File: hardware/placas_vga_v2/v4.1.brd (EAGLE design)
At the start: 32 x 39.9 mm, 39 parts

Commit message: Finalizo diseño
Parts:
- moved R2 0.64 mm to (18.8, 22.9)
- moved R22 0.64 mm to (18.8, 25.3)
- moved R3 0.64 mm to (18.8, 18.2)
- moved R6 0.64 mm to (18.8, 3.89)
- moved R7 0.64 mm to (18.8, 1.51)
- moved R24 0.63 mm to (18.8, 15.8)
- moved R25 0.63 mm to (18.8, 11.0)
- moved R26 0.63 mm to (18.8, 6.27)
- moved R4 0.63 mm to (18.8, 13.4)
- moved R5 0.63 mm to (18.8, 8.65)
- moved R1 0.63 mm to (18.8, 27.7), turned to 180 degrees
- moved R23 0.63 mm to (18.8, 20.6)
- moved R10 0.48 mm to (23.7, 18.3)
- moved R11 0.48 mm to (23.7, 13.6)
- moved R12 0.48 mm to (23.7, 8.81)
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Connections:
- removed net EXT11: R16.1
- removed net EXT14: R15.1
- removed net EXT2: R8.1
- removed net EXT3: R10.1
- removed net EXT4: R9.1
- removed net EXT5: R17.1
- removed net N$1: U$1.10, U$1.5, U$1.6, U$1.7, U$1.8, U$1.9
- removed net N$10: R12.1
- removed net N$11: R13.1
- removed net N$12: R18.1
- removed net N$13: R19.1
- removed net N$14: R20.1
- removed net N$9: R11.1
- net EXT18: now also R8.1
- net EXT19: now also R9.1
- net EXT21: now also R10.1
- net EXT22: now also R11.1
- net EXT24: now also R12.1
- net EXT25: now also R13.1
- net EXT27: now also R17.1
- net EXT28: now also R15.1
- net EXT30: now also R18.1
- net EXT31: now also R16.1
- net EXT33: now also R20.1
- net EXT34: now also R19.1
- net GND: now also U$1.10, U$1.5, U$1.6, U$1.7, U$1.8
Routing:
- net GND: track 12.4 -> 89.6 mm
- net EXT33: track 0.00 -> 37.4 mm
- net EXT24: track 0.00 -> 36.1 mm
- net EXT25: track 0.00 -> 34.2 mm
- net EXT30: track 0.00 -> 29.1 mm
- net EXT21: track 0.00 -> 28.2 mm
- net EXT34: track 0.00 -> 26.4 mm
- net EXT22: track 0.00 -> 26.2 mm
- net EXT27: track 0.00 -> 26.2 mm
- net N$41: track 2.38 -> 21.0 mm, vias 0 -> 1
- net EXT18: track 0.00 -> 18.5 mm
- net EXT19: track 0.00 -> 18.3 mm
- net EXT31: track 0.00 -> 13.1 mm
- net GREEN: track 2.38 -> 15.4 mm, vias 0 -> 1
- net EXT28: track 0.00 -> 8.75 mm
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- added copper zone on layer 1, net GND

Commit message: Añado sd2iec
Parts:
- renumbered U$1 to VGA
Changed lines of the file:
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@@
 <element name="J12" library="pinhead" package="1X12" value="" x="16.51" y="32.940625"/>
 <element name="J10" library="pinhead" package="1X12" value="" x="16.51" y="38.020625"/>
-<element name="U$1" library="SparkFun-Connectors" package="DB15" value="DB15" x="6.6675" y="15.478125" rot="MR270"/>
+<element name="VGA" library="SparkFun-Connectors" package="DB15" value="DB15" x="6.6675" y="15.478125" rot="MR270"/>
 <element name="R1" library="rcl" package="R0805" value="511" x="18.811875" y="27.701875" rot="MR180"/>
 <element name="R2" library="rcl" package="R0805" value="511" x="18.811875" y="22.939375" rot="MR0"/>
@@
 <wire x1="24.683125" y1="1.666875" x2="24.683125" y2="0.875625" width="0.254" layer="16"/>
 <wire x1="24.683125" y1="0.875625" x2="24.685625" y2="0.873125" width="0.254" layer="16"/>
-<contactref element="U$1" pad="7"/>
-<contactref element="U$1" pad="8"/>
-<contactref element="U$1" pad="10"/>
-<contactref element="U$1" pad="5"/>
-<contactref element="U$1" pad="6"/>
+<contactref element="VGA" pad="7"/>
+<contactref element="VGA" pad="8"/>
+<contactref element="VGA" pad="10"/>
+<contactref element="VGA" pad="5"/>
+<contactref element="VGA" pad="6"/>
 <wire x1="14.2875" y1="10.638125" x2="12.8875" y2="10.638125" width="0.254" layer="16"/>
 <wire x1="12.8875" y1="10.638125" x2="11.7475" y2="11.778125" width="0.254" layer="16"/>
@@
 </signal>
 <signal name="GREEN">
-<contactref element="U$1" pad="2"/>
+<contactref element="VGA" pad="2"/>
 <contactref element="R8" pad="2"/>
 <contactref element="R27" pad="1"/>
@@
 </signal>
 <signal name="HSYNC">
-<contactref element="U$1" pad="13"/>
+<contactref element="VGA" pad="13"/>
 <contactref element="J12" pad="2"/>
 <wire x1="5.08" y1="32.940625" x2="5.08" y2="19.345625" width="0.254" layer="16"/>
@@
 </signal>
 <signal name="VSYNC">
-<contactref element="U$1" pad="14"/>
+<contactref element="VGA" pad="14"/>
 <contactref element="J10" pad="1"/>
 <wire x1="2.54" y1="38.020625" x2="2.54" y2="34.925" width="0.254" layer="16"/>
@@
 </signal>
 <signal name="N$16">
-<contactref element="U$1" pad="1"/>
+<contactref element="VGA" pad="1"/>
 <contactref element="R1" pad="2"/>
 <contactref element="R22" pad="1"/>
@@
 <signal name="N$41">
 <contactref element="R15" pad="2"/>
-<contactref element="U$1" pad="3"/>
+<contactref element="VGA" pad="3"/>
 <contactref element="R32" pad="1"/>
 <wire x1="27.704375" y1="28.336875" x2="27.704375" y2="25.955625" width="0.254" layer="16"/>

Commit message: Actualizo varios
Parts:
- moved J10 0.32 mm to (16.2, 38.0)
- moved J12 0.32 mm to (16.2, 32.9)
- moved R10 0.32 mm to (23.4, 18.3)
- moved R11 0.32 mm to (23.4, 13.6)
- moved R12 0.32 mm to (23.4, 8.81)
- moved R13 0.32 mm to (23.4, 4.05)
- moved R14 0.32 mm to (23.4, 1.67)
- moved R15 0.32 mm to (28.3, 28.3)
- moved R16 0.32 mm to (28.3, 23.1)
- moved R17 0.32 mm to (28.3, 18.3)
- moved R18 0.32 mm to (28.3, 13.6)
- moved R19 0.32 mm to (28.3, 8.81)
- moved R20 0.32 mm to (28.3, 4.05)
- moved R21 0.32 mm to (28.3, 1.67)
- moved R27 0.32 mm to (23.4, 26.0)
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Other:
- board size 32 x 39.9 mm -> 31.7 x 39.5 mm

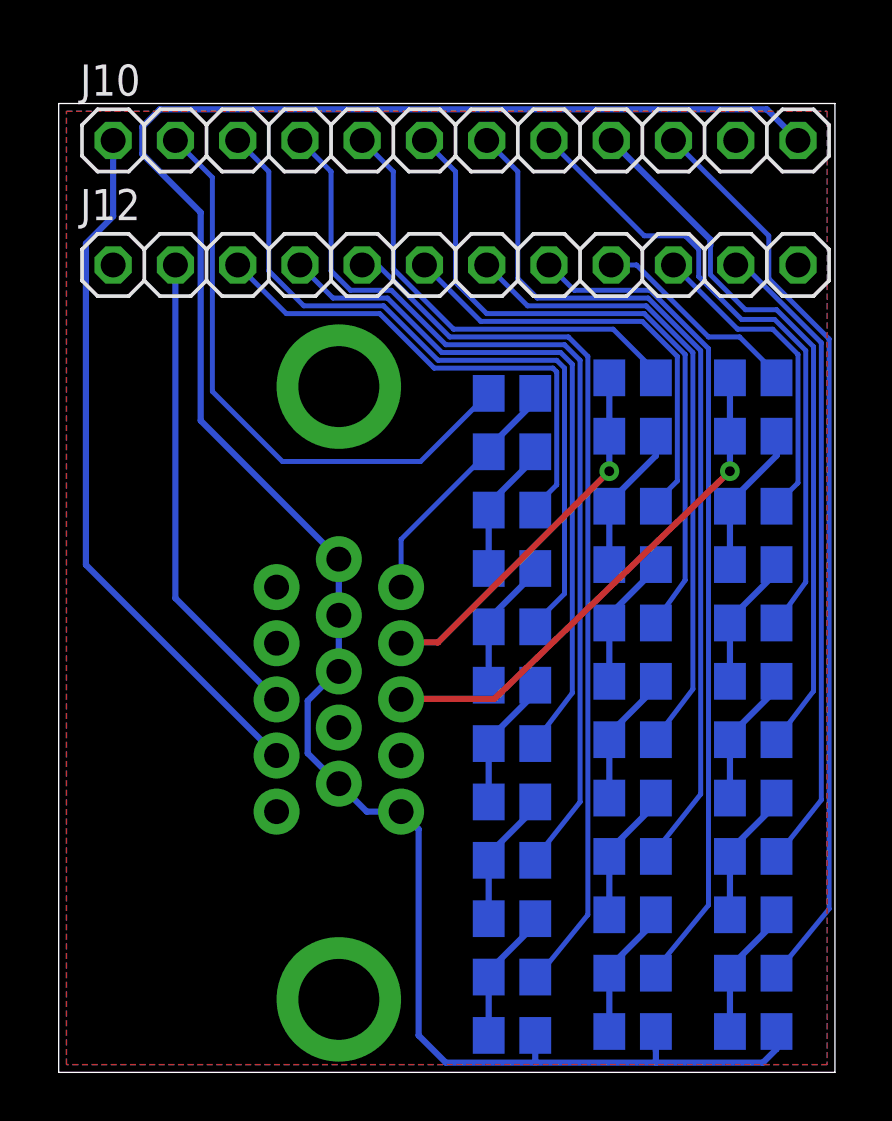
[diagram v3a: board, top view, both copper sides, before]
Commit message: Actualizo diseño DAC 18 bits
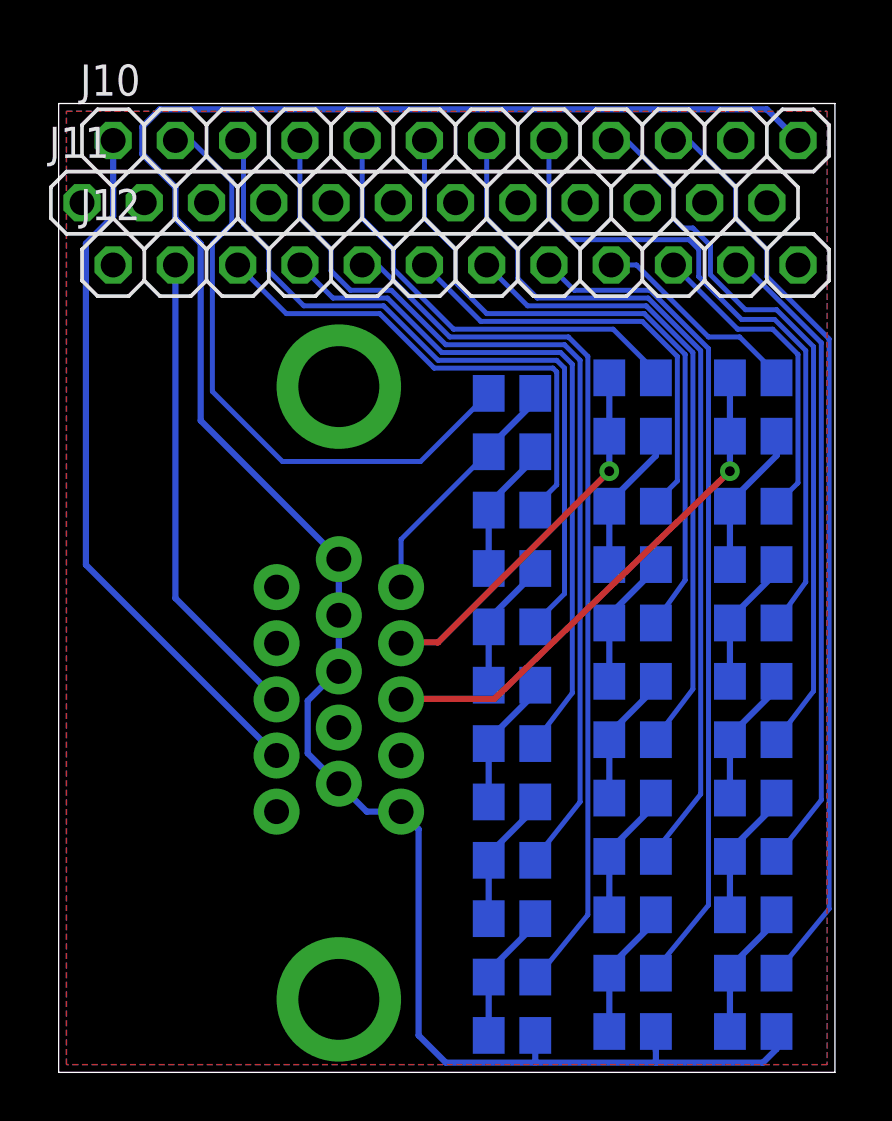
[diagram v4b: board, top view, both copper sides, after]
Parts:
- added J11: (no value), pinhead:1X12
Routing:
- net EXT27: track 26.2 -> 28.0 mm
- net EXT9: track 24.5 -> 25.5 mm
- net EXT30: track 29.1 -> 29.7 mm
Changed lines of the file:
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@@
 <element name="R36" library="rcl" package="R0805" value="255" x="28.336875" y="6.429375" rot="MR180"/>
 <element name="R21" library="rcl" package="R0805" value="511" x="28.336875" y="1.666875" rot="MR180"/>
+<element name="J11" library="pinhead" package="1X12" value="" x="14.9225" y="35.480625"/>
 </elements>
 <signals>
@@
 <wire x1="11.43" y1="20.938125" x2="11.43" y2="20.955" width="0.254" layer="16"/>
 <wire x1="11.43" y1="20.955" x2="5.794375" y2="26.590625" width="0.254" layer="16"/>
-<wire x1="5.794375" y1="26.590625" x2="5.794375" y2="35.08375" width="0.254" layer="16"/>
-<wire x1="5.794375" y1="35.08375" x2="3.413125" y2="37.465" width="0.254" layer="16"/>
 <wire x1="3.413125" y1="37.465" x2="3.413125" y2="38.57625" width="0.254" layer="16"/>
 <wire x1="3.413125" y1="38.57625" x2="4.1275" y2="39.290625" width="0.254" layer="16"/>
@@
 <vertex x="0.3175" y="0.3175"/>
 </polygon>
+<wire x1="5.794375" y1="26.590625" x2="5.794375" y2="33.81375" width="0.254" layer="16"/>
+<wire x1="5.794375" y1="33.81375" x2="4.7625" y2="34.845625" width="0.254" layer="16"/>
+<wire x1="4.7625" y1="34.845625" x2="4.7625" y2="36.115625" width="0.254" layer="16"/>
+<wire x1="4.7625" y1="36.115625" x2="3.413125" y2="37.465" width="0.254" layer="16"/>
 </signal>
 <signal name="EXT9">
@@
 <wire x1="14.76625" y1="24.92375" x2="9.128125" y2="24.92375" width="0.2032" layer="16"/>
 <wire x1="9.128125" y1="24.92375" x2="6.270625" y2="27.78125" width="0.2032" layer="16"/>
-<wire x1="6.270625" y1="27.78125" x2="6.270625" y2="36.5125" width="0.2032" layer="16"/>
-<wire x1="6.270625" y1="36.5125" x2="4.7625" y2="38.020625" width="0.2032" layer="16"/>
 <wire x1="14.76625" y1="24.92375" x2="17.544375" y2="27.701875" width="0.2032" layer="16"/>
+<wire x1="6.270625" y1="27.78125" x2="6.270625" y2="33.81375" width="0.2032" layer="16"/>
+<wire x1="6.270625" y1="33.81375" x2="7.064375" y2="34.6075" width="0.2032" layer="16"/>
+<wire x1="7.064375" y1="34.6075" x2="7.064375" y2="36.35375" width="0.2032" layer="16"/>
+<wire x1="7.064375" y1="36.35375" x2="5.3975" y2="38.020625" width="0.2032" layer="16"/>
+<wire x1="4.7625" y1="38.020625" x2="5.3975" y2="38.020625" width="0.2032" layer="16"/>
 </signal>
 <signal name="EXT10">
@@
 <wire x1="13.255625" y1="31.27375" x2="10.00125" y2="31.27375" width="0.2032" layer="16"/>
 <wire x1="10.00125" y1="31.27375" x2="8.5725" y2="32.7025" width="0.2032" layer="16"/>
-<wire x1="8.5725" y1="32.7025" x2="8.5725" y2="36.750625" width="0.2032" layer="16"/>
-<wire x1="8.5725" y1="36.750625" x2="7.3025" y2="38.020625" width="0.2032" layer="16"/>
 <wire x1="20.6375" y1="28.73375" x2="20.32" y2="29.05125" width="0.2032" layer="16"/>
+<wire x1="7.3025" y1="38.020625" x2="7.540625" y2="37.7825" width="0.2032" layer="16"/>
+<wire x1="7.540625" y1="37.7825" x2="7.540625" y2="34.6075" width="0.2032" layer="16"/>
+<wire x1="7.540625" y1="34.6075" x2="8.5725" y2="33.575625" width="0.2032" layer="16"/>
+<wire x1="8.5725" y1="33.575625" x2="8.5725" y2="32.7025" width="0.2032" layer="16"/>
 </signal>
 <signal name="EXT13">
@@
 <wire x1="13.573125" y1="31.90875" x2="11.90625" y2="31.90875" width="0.2032" layer="16"/>
 <wire x1="11.90625" y1="31.90875" x2="11.1125" y2="32.7025" width="0.2032" layer="16"/>
-<wire x1="11.1125" y1="32.7025" x2="11.1125" y2="36.750625" width="0.2032" layer="16"/>
-<wire x1="11.1125" y1="36.750625" x2="9.8425" y2="38.020625" width="0.2032" layer="16"/>
+<wire x1="9.8425" y1="38.020625" x2="9.8425" y2="34.845625" width="0.2032" layer="16"/>
+<wire x1="9.8425" y1="34.845625" x2="11.1125" y2="33.575625" width="0.2032" layer="16"/>
+<wire x1="11.1125" y1="33.575625" x2="11.1125" y2="32.7025" width="0.2032" layer="16"/>
 </signal>
 <signal name="EXT16">
@@
 <wire x1="22.621875" y1="30.32125" x2="16.113125" y2="30.32125" width="0.2032" layer="16"/>
 <wire x1="16.113125" y1="30.32125" x2="13.6525" y2="32.781875" width="0.2032" layer="16"/>
-<wire x1="13.6525" y1="32.781875" x2="13.6525" y2="36.750625" width="0.2032" layer="16"/>
-<wire x1="13.6525" y1="36.750625" x2="12.3825" y2="38.020625" width="0.2032" layer="16"/>
+<wire x1="12.3825" y1="38.020625" x2="12.3825" y2="34.845625" width="0.2032" layer="16"/>
+<wire x1="12.3825" y1="34.845625" x2="13.6525" y2="33.575625" width="0.2032" layer="16"/>
+<wire x1="13.6525" y1="33.575625" x2="13.6525" y2="32.781875" width="0.2032" layer="16"/>
 </signal>
 <signal name="EXT19">
@@
 <wire x1="23.891875" y1="30.95625" x2="17.4625" y2="30.95625" width="0.2032" layer="16"/>
 <wire x1="17.4625" y1="30.95625" x2="16.1925" y2="32.22625" width="0.2032" layer="16"/>
-<wire x1="16.1925" y1="32.22625" x2="16.1925" y2="36.750625" width="0.2032" layer="16"/>
-<wire x1="16.1925" y1="36.750625" x2="14.9225" y2="38.020625" width="0.2032" layer="16"/>
+<wire x1="14.9225" y1="38.020625" x2="14.9225" y2="34.845625" width="0.2032" layer="16"/>
+<wire x1="14.9225" y1="34.845625" x2="16.1925" y2="33.575625" width="0.2032" layer="16"/>
+<wire x1="16.1925" y1="33.575625" x2="16.1925" y2="32.22625" width="0.2032" layer="16"/>
 </signal>
 <signal name="EXT22">
@@
 <wire x1="24.050625" y1="31.59125" x2="19.52625" y2="31.59125" width="0.2032" layer="16"/>
 <wire x1="19.52625" y1="31.59125" x2="18.7325" y2="32.385" width="0.2032" layer="16"/>
-<wire x1="18.7325" y1="32.385" x2="18.7325" y2="36.750625" width="0.2032" layer="16"/>
-<wire x1="18.7325" y1="36.750625" x2="17.4625" y2="38.020625" width="0.2032" layer="16"/>
+<wire x1="17.4625" y1="38.020625" x2="17.4625" y2="34.845625" width="0.2032" layer="16"/>
+<wire x1="17.4625" y1="34.845625" x2="18.7325" y2="33.575625" width="0.2032" layer="16"/>
+<wire x1="18.7325" y1="33.575625" x2="18.7325" y2="32.385" width="0.2032" layer="16"/>
 </signal>
 <signal name="EXT25">
@@
 <contactref element="J10" pad="8"/>
 <contactref element="R17" pad="1"/>
-<wire x1="20.0025" y1="38.020625" x2="23.891875" y2="34.13125" width="0.2032" layer="16"/>
-<wire x1="23.891875" y1="34.13125" x2="25.55875" y2="34.13125" width="0.2032" layer="16"/>
-<wire x1="25.55875" y1="34.13125" x2="26.114375" y2="33.575625" width="0.2032" layer="16"/>
 <wire x1="26.114375" y1="33.575625" x2="26.114375" y2="32.464375" width="0.2032" layer="16"/>
 <wire x1="26.114375" y1="32.464375" x2="27.860625" y2="30.718125" width="0.2032" layer="16"/>
@@
 <wire x1="30.48" y1="29.448125" x2="30.48" y2="20.005" width="0.2032" layer="16"/>
 <wire x1="30.48" y1="20.005" x2="29.286875" y2="18.335625" width="0.2032" layer="16"/>
+<wire x1="20.0025" y1="38.020625" x2="20.0025" y2="34.845625" width="0.2032" layer="16"/>
+<wire x1="20.0025" y1="34.845625" x2="20.875625" y2="33.9725" width="0.2032" layer="16"/>
+<wire x1="20.875625" y1="33.9725" x2="25.7175" y2="33.9725" width="0.2032" layer="16"/>
+<wire x1="25.7175" y1="33.9725" x2="26.114375" y2="33.575625" width="0.2032" layer="16"/>
 </signal>
 <signal name="EXT28">
@@
 <contactref element="J10" pad="9"/>
 <contactref element="R18" pad="1"/>
-<wire x1="26.590625" y1="33.734375" x2="26.590625" y2="32.54375" width="0.2032" layer="16"/>
 <wire x1="26.590625" y1="32.54375" x2="28.019375" y2="31.115" width="0.2032" layer="16"/>
 <wire x1="28.019375" y1="31.115" x2="29.289375" y2="31.115" width="0.2032" layer="16"/>
@@
 <wire x1="30.7975" y1="29.606875" x2="30.7975" y2="15.56" width="0.2032" layer="16"/>
 <wire x1="30.7975" y1="15.56" x2="29.286875" y2="13.573125" width="0.2032" layer="16"/>
-<wire x1="26.590625" y1="33.734375" x2="26.590625" y2="33.9725" width="0.254" layer="16"/>
-<wire x1="26.590625" y1="33.9725" x2="22.5425" y2="38.020625" width="0.254" layer="16"/>
+<wire x1="26.590625" y1="32.54375" x2="26.590625" y2="33.734375" width="0.2032" layer="16"/>
+<wire x1="26.590625" y1="33.734375" x2="25.87625" y2="34.44875" width="0.2032" layer="16"/>
+<wire x1="25.87625" y1="34.44875" x2="25.479375" y2="34.44875" width="0.2032" layer="16"/>
+<wire x1="25.479375" y1="34.44875" x2="25.0825" y2="34.845625" width="0.2032" layer="16"/>
+<wire x1="25.0825" y1="34.845625" x2="25.0825" y2="36.115625" width="0.2032" layer="16"/>
+<wire x1="25.0825" y1="36.115625" x2="23.1775" y2="38.020625" width="0.2032" layer="16"/>
+<wire x1="23.1775" y1="38.020625" x2="22.5425" y2="38.020625" width="0.2032" layer="16"/>
 </signal>
 <signal name="EXT31">
@@
 <contactref element="J10" pad="10"/>
 <contactref element="R20" pad="1"/>
-<wire x1="25.0825" y1="38.020625" x2="28.971875" y2="34.13125" width="0.2032" layer="16"/>
-<wire x1="28.971875" y1="34.13125" x2="28.971875" y2="32.385" width="0.2032" layer="16"/>
-<wire x1="28.971875" y1="32.385" x2="31.4325" y2="29.924375" width="0.2032" layer="16"/>
+<wire x1="28.8925" y1="32.464375" x2="31.4325" y2="29.924375" width="0.2032" layer="16"/>
 <wire x1="31.4325" y1="29.924375" x2="31.4325" y2="6.67" width="0.2032" layer="16"/>
 <wire x1="31.4325" y1="6.67" x2="29.286875" y2="4.048125" width="0.2032" layer="16"/>
+<wire x1="25.0825" y1="38.020625" x2="25.7175" y2="38.020625" width="0.2032" layer="16"/>
+<wire x1="25.7175" y1="38.020625" x2="27.6225" y2="36.115625" width="0.2032" layer="16"/>
+<wire x1="27.6225" y1="36.115625" x2="27.6225" y2="34.845625" width="0.2032" layer="16"/>
+<wire x1="27.6225" y1="34.845625" x2="28.8925" y2="33.575625" width="0.2032" layer="16"/>
+<wire x1="28.8925" y1="33.575625" x2="28.8925" y2="32.464375" width="0.2032" layer="16"/>
 </signal>
 <signal name="EXT34">
